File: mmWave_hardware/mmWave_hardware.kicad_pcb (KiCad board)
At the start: 2 copper layers, 1 part, among them U1 IWRL6432BDBAAMFR

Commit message: sch+pcb
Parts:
- added C1: 10p, Capacitor_SMD:C_0402_1005Metric_Pad0.74x0.62mm_HandSolder, B.Cu at (176.4, 112.5)
- added C10: 2u2, Capacitor_SMD:C_0603_1608Metric_Pad1.08x0.95mm_HandSolder, B.Cu at (181.3, 110.2)
- added C11: 10u, Capacitor_SMD:C_0603_1608Metric_Pad1.08x0.95mm_HandSolder, F.Cu at (177.8, 81.0)
- added C12: 2u2, Capacitor_SMD:C_0603_1608Metric_Pad1.08x0.95mm_HandSolder, F.Cu at (177.8, 83.5)
- added C13: 10u, Capacitor_SMD:C_0603_1608Metric_Pad1.08x0.95mm_HandSolder, B.Cu at (187.0, 118.3)
- added C14: 2u2, Capacitor_SMD:C_0603_1608Metric_Pad1.08x0.95mm_HandSolder, B.Cu at (187.0, 116.8)
- added C15: 47n, Capacitor_SMD:C_0402_1005Metric_Pad0.74x0.62mm_HandSolder, F.Cu at (179.8, 95.4)
- added C16: 1u, Capacitor_SMD:C_0603_1608Metric_Pad1.08x0.95mm_HandSolder, F.Cu at (182.1, 78.5)
- added C17: 1u, Capacitor_SMD:C_0603_1608Metric_Pad1.08x0.95mm_HandSolder, F.Cu at (182.1, 81.0)
- added C18: 10u, Capacitor_SMD:C_0603_1608Metric, F.Cu at (187.2, 106.4)
- added C19: 10u, Capacitor_SMD:C_0603_1608Metric, F.Cu at (193.6, 101.9)
- added C2: 10p, Capacitor_SMD:C_0402_1005Metric_Pad0.74x0.62mm_HandSolder, B.Cu at (176.5, 105.4)
- added C20: 10u, Capacitor_SMD:C_0603_1608Metric, F.Cu at (176.2, 91.0)
- added C21: 2u2, Capacitor_SMD:C_0603_1608Metric, F.Cu at (176.2, 93.5)
- added C3: 10u, Capacitor_SMD:C_0603_1608Metric_Pad1.08x0.95mm_HandSolder, B.Cu at (186.0, 112.2)
- added C4: 2u2, Capacitor_SMD:C_0603_1608Metric_Pad1.08x0.95mm_HandSolder, B.Cu at (186.0, 110.5)
- added C5: 10u, Capacitor_SMD:C_0603_1608Metric_Pad1.08x0.95mm_HandSolder, F.Cu at (178.9, 119.2)
- added C6: 2u2, Capacitor_SMD:C_0603_1608Metric_Pad1.08x0.95mm_HandSolder, F.Cu at (180.6, 119.2)
- added C7: 10u, Capacitor_SMD:C_0603_1608Metric_Pad1.08x0.95mm_HandSolder, F.Cu at (183.0, 119.1)
- added C8: 2u2, Capacitor_SMD:C_0603_1608Metric_Pad1.08x0.95mm_HandSolder, F.Cu at (184.8, 119.2)
- added C9: 10u, Capacitor_SMD:C_0603_1608Metric_Pad1.08x0.95mm_HandSolder, B.Cu at (183.0, 110.2)
- added J1: Conn_02x08_Top_Bottom, Connector_PinHeader_2.54mm:PinHeader_2x08_P2.54mm_Vertical, F.Cu at (209.4, 104.9)
- added R1: 10k, Resistor_SMD:R_0402_1005Metric, F.Cu at (172.7, 85.8)
- added R2: 100k, Resistor_SMD:R_0402_1005Metric, F.Cu at (172.7, 87.7)
- added R3: 100k, Resistor_SMD:R_0402_1005Metric, F.Cu at (172.7, 89.7)
- added R4: 10k, Resistor_SMD:R_0402_1005Metric, F.Cu at (172.7, 91.7)
- added R5: 10k, Resistor_SMD:R_0402_1005Metric, F.Cu at (172.7, 93.7)
- added R6: 10k, Resistor_SMD:R_0402_1005Metric, F.Cu at (172.7, 95.7)
- added TP1: TestPoint, TestPoint:TestPoint_Pad_D2.0mm, F.Cu at (161.6, 74.7)
- added TP2: TestPoint, TestPoint:TestPoint_Pad_D2.0mm, F.Cu at (161.6, 79.8)
- added TP3: TestPoint, TestPoint:TestPoint_Pad_D2.0mm, F.Cu at (161.6, 84.8)
- added TP4: TestPoint, TestPoint:TestPoint_Pad_D2.0mm, F.Cu at (161.6, 89.9)
- added TP5: TestPoint, TestPoint:TestPoint_Pad_D2.0mm, B.Cu at (189.5, 121.3)
- added U2: W25Q128JVS, Package_SO:SOIC-8_5.3x5.3mm_P1.27mm, F.Cu at (195.5, 108.1)
- added U3: AMS1117-3.3, Package_TO_SOT_SMD:SOT-223-3_TabPin2, F.Cu at (187.4, 101.1)
- added U4: TPS5430DDA, Package_SO:TI_SO-PowerPAD-8_ThermalVias, F.Cu at (147.1, 80.0)
- added Y1: 40.000, Crystal:Crystal_SMD_3225-4Pin_3.2x2.5mm_HandSoldering, B.Cu at (176.4, 109.0)
- moved U1 72.8 mm to (183.6, 113.5)
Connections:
- net Net-(U1-VSSA_PM) renamed GND
- U1 pad A10: unconnected-(U1-QSPI_CS-PadA10) -> /QSPI_CS
- U1 pad A11: unconnected-(U1-QSPI_CLK-PadA11) -> /QSPI_CLK
- U1 pad A3: unconnected-(U1-TX1-PadA3) -> TX1
- U1 pad A5: unconnected-(U1-TX2-PadA5) -> TX2
- U1 pad A7: unconnected-(U1-OSC_CLK_OUT-PadA7) -> Net-(U1-OSC_CLK_OUT)
- U1 pad B10: unconnected-(U1-QSPI[2]-PadB10) -> /QSPI_2
- U1 pad B11: unconnected-(U1-QSPI[0]-PadB11) -> /QSPI_0
- U1 pad B12: unconnected-(U1-SPIA_MOSI-PadB12) -> SPI0_MOSI
- U1 pad B8: unconnected-(U1-QSPI[1]-PadB8) -> /QSPI_2
- U1 pad B9: unconnected-(U1-QSPI[3]-PadB9) -> /QSPI_3
- U1 pad C11: unconnected-(U1-SPIA_MISO-PadC11) -> SPI0_MISO
- U1 pad C12: unconnected-(U1-TCK-PadC12) -> TCK
- U1 pad C6: unconnected-(U1-VIOIN_I8CLK-PadC6) -> 1v8
- U1 pad C8: unconnected-(U1-VIOIN_18-PadC8) -> 1v8
- U1 pad C9: unconnected-(U1-VDD-PadC9) -> 1v2
- U1 pad D10: unconnected-(U1-SPIA_CLK-PadD10) -> SPI0_CLK
- U1 pad D11: unconnected-(U1-SPIA_CS0_N-PadD11) -> SPI0_CS0_N
- U1 pad D3: unconnected-(U1-VOUT_14SYNTH-PadD3) -> Net-(U1-VOUT_14SYNTH)
- U1 pad E10: unconnected-(U1-RS232_TX-PadE10) -> RS232_TX
- U1 pad E11: unconnected-(U1-TDO-PadE11) -> TDO
- U1 pad E12: unconnected-(U1-TMS-PadE12) -> TMS
- U1 pad F1: unconnected-(U1-RX3-PadF1) -> RX3
- U1 pad F11: unconnected-(U1-RS232_RX-PadF11) -> RS232_RX
- U1 pad F3: unconnected-(U1-VDDA_18VCO-PadF3) -> 1v8
- U1 pad G11: unconnected-(U1-TDI-PadG11) -> TDI
- U1 pad G12: unconnected-(U1-VIOIN-PadG12) -> 3v3
- U1 pad G5: unconnected-(U1-VOUT_14APLL-PadG5) -> Net-(U1-VOUT_14APLL)
- U1 pad G7: unconnected-(U1-VDD-PadG7) -> 1v2
- U1 pad G8: unconnected-(U1-VDD-PadG8) -> 1v2
- U1 pad G9: unconnected-(U1-VDD-PadG9) -> 1v2
- U1 pad H1: unconnected-(U1-RX2-PadH1) -> RX2
- U1 pad H10: unconnected-(U1-GPIO_2-PadH10) -> GPIO_2
- U1 pad H11: unconnected-(U1-PMIC_CLKOUT-PadH11) -> Net-(U1-PMIC_CLKOUT)
- U1 pad H5: unconnected-(U1-VBGAP-PadH5) -> Net-(U1-VBGAP)
- U1 pad H8: unconnected-(U1-VDD-PadH8) -> 1v2
- U1 pad J10: unconnected-(U1-GPIO_5-PadJ10) -> GPIO_5
- U1 pad J11: unconnected-(U1-UARTA_RX-PadJ11) -> UART_RX
- U1 pad J5: unconnected-(U1-VIN_18PM-PadJ5) -> 1v8
- U1 pad K1: unconnected-(U1-RX1-PadK1) -> RX1
- U1 pad K11: unconnected-(U1-NERROR_OUT-PadK11) -> Net-(U1-NERROR_OUT)
- U1 pad K12: unconnected-(U1-VIOIN_18-PadK12) -> 1v8
- U1 pad K7: unconnected-(U1-VDD-PadK7) -> 1v2
- U1 pad L10: unconnected-(U1-NRESET-PadL10) -> NRST_MAIN
- U1 pad L11: unconnected-(U1-UARTA_RTS-PadL11) -> UART_RTS
- U1 pad L12: unconnected-(U1-UARTA_TX-PadL12) -> UART_TX
- U1 pad L3: unconnected-(U1-VDDA_10RF-PadL3) -> Net-(C5-Pad2)
- U1 pad L4: unconnected-(U1-VDDA_12RF-PadL4) -> Net-(C7-Pad1)
- U1 pad L5: unconnected-(U1-VDDA_18BB-PadL5) -> 1v8
- U1 pad L6: unconnected-(U1-GPADC2-PadL6) -> Net-(U1-GPADC2)
- U1 pad L8: unconnected-(U1-VIOIN_18-PadL8) -> 1v8
- U1 pad L9: unconnected-(U1-VNWA-PadL9) -> VDD_SRAM
- U1 pad M10: unconnected-(U1-HOST_CLK_REQ-PadM10) -> Net-(U1-HOST_CLK_REQ)
- U1 pad M11: unconnected-(U1-VIOIN-PadM11) -> 3v3
- U1 pad M3: unconnected-(U1-VDDA_10RF-PadM3) -> Net-(C5-Pad2)
- U1 pad M4: unconnected-(U1-VDDA_12RF-PadM4) -> Net-(C7-Pad1)
- U1 pad M5: unconnected-(U1-VDDA_18BB-PadM5) -> 1v8
- U1 pad M6: unconnected-(U1-GPADC1-PadM6) -> Net-(U1-GPADC1)
- U1 pad M7: unconnected-(U1-VDD_SRAM-PadM7) -> VDD_SRAM
- U1 pad M8: unconnected-(U1-VIOIN_18-PadM8) -> 1v8
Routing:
- net GND: track 13.0 -> 25.0 mm, vias 0 -> 9
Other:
- copper layers 2 -> 6

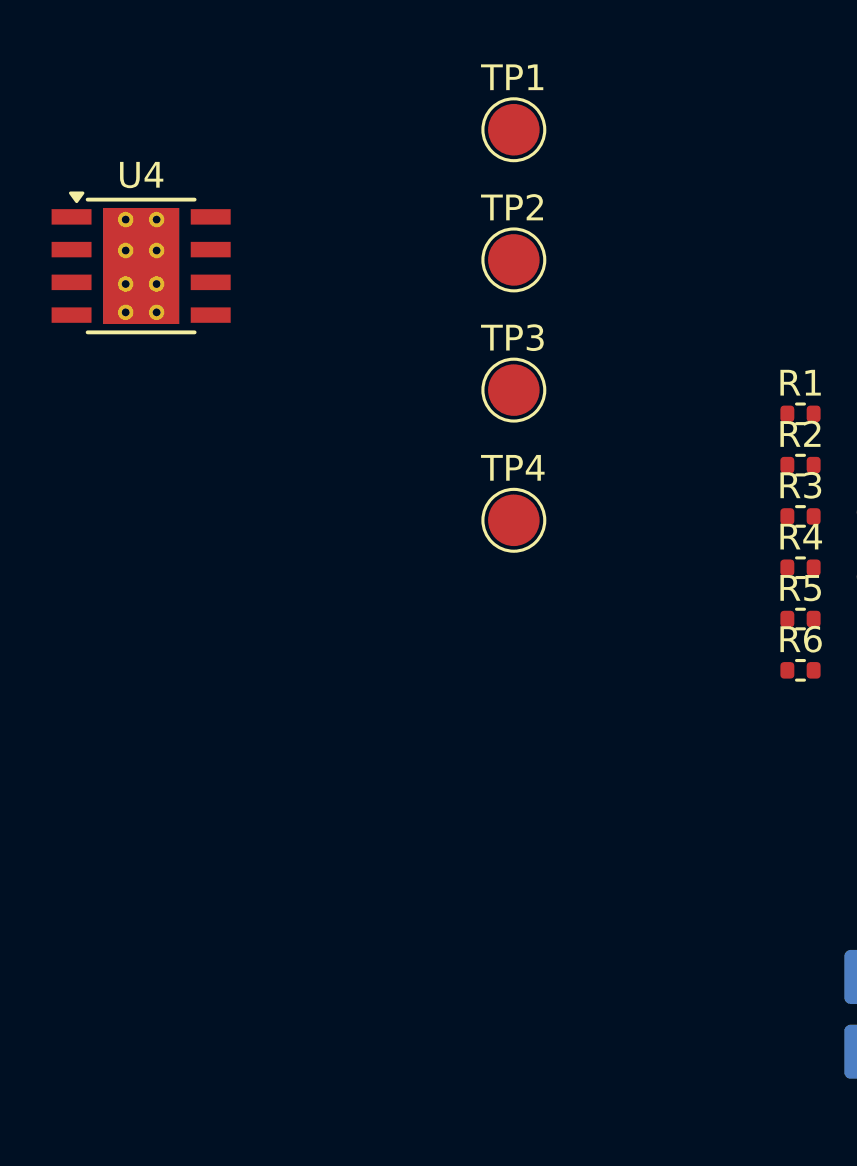
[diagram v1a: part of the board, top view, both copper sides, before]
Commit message: new buck conv
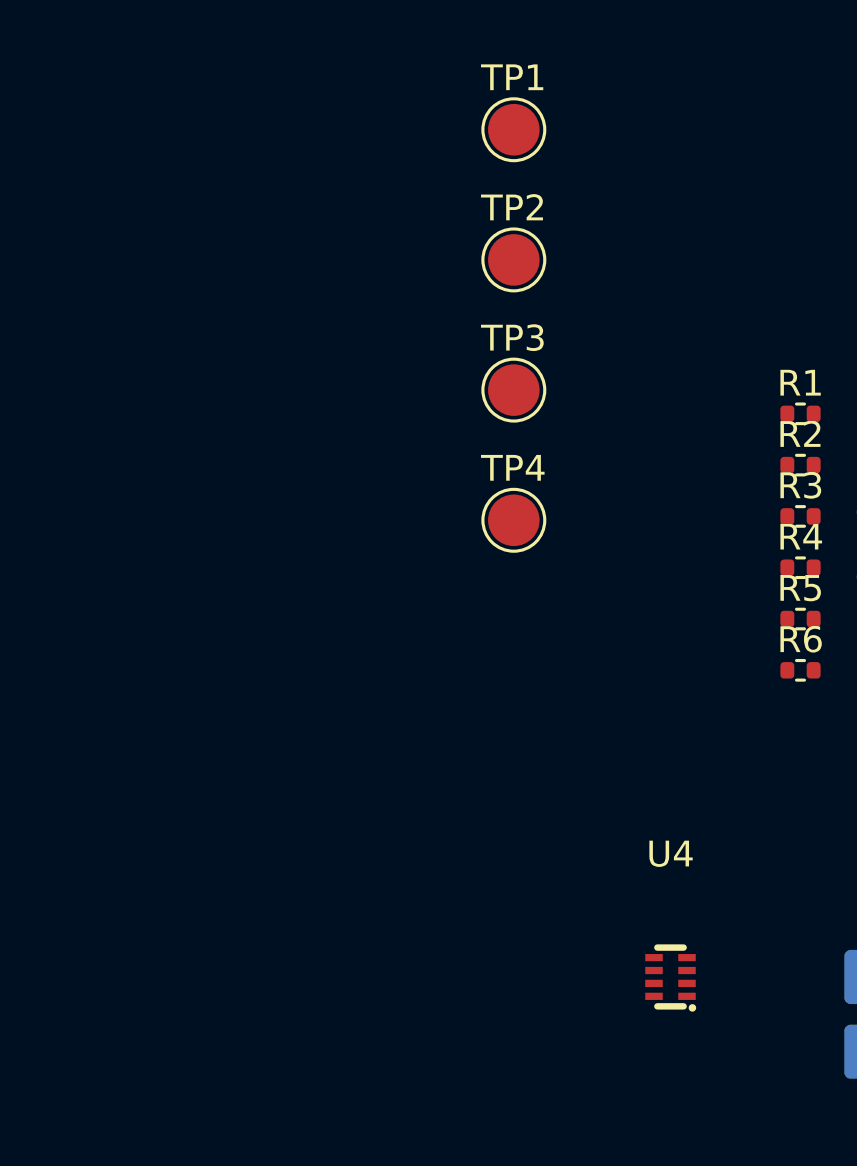
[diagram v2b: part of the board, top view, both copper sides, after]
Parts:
- C1, C2: value 10p -> 15p
- U4: value TPS5430DDA -> TPS628502QDRLRQ1; footprint Package_SO:TI_SO-PowerPAD-8_ThermalVias -> easyeda2kicad:SOT-583-8_L2.1-W1.2-P0.50-LS1.6-BR
- moved U4 34.4 mm to (167.7, 107.6)
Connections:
- U4 pad 1: unconnected-(U4-BOOT-Pad1) -> VIN
- U4 pad 2: unconnected-(U4-NC-Pad2) -> VIN
- U4 pad 5: VIN -> unconnected-(U4-FB-Pad5)
- U4 pad 6: GND -> unconnected-(U4-PG-Pad6)
- U4 pad 7: VIN -> unconnected-(U4-SW-Pad7)

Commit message: sch
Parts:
- C10, C13, C14, C3, C4, C9: moved to F.Cu
- C15: moved to B.Cu
- moved C15 20.3 mm to (183.8, 115.3), turned to 180 degrees
- moved C3 16.2 mm to (171.6, 119.5), turned to 180 degrees
- moved C4 16.2 mm to (171.6, 117.8), turned to 180 degrees
- moved C9 13.0 mm to (170.8, 114.7)
- moved C10 9.91 mm to (172.5, 114.7)
- moved C14 4.13 mm to (184.5, 120.1), turned to -90 degrees
- moved C8 2.06 mm to (182.9, 120.1)
- moved C13 2.06 mm to (186.2, 120.2), turned to -90 degrees
- moved C7 1.94 mm to (181.3, 120.1)
- moved C6 1.28 mm to (179.7, 120.1)
- moved C5 1.21 mm to (178.1, 120.1)
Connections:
- U1 pad B8: /QSPI_2 -> /QSPI_1
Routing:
- net GND: track 25.0 -> 12.6 mm, vias 9 -> 1
- net 1v8: track 0.00 -> 8.75 mm
- net Net-(C5-Pad2): track 0.00 -> 5.93 mm
- net Net-(C7-Pad1): track 0.00 -> 3.86 mm
- net 1v2: track 0.00 -> 1.50 mm

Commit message: sch+pcb
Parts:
- added C22: 10u, Capacitor_SMD:C_0603_1608Metric_Pad1.08x0.95mm_HandSolder, F.Cu at (196.7, 81.8)
- added C23: 10u, Capacitor_SMD:C_0603_1608Metric_Pad1.08x0.95mm_HandSolder, F.Cu at (196.7, 84.3)
- added C24: 10u, Capacitor_SMD:C_0603_1608Metric_Pad1.08x0.95mm_HandSolder, F.Cu at (196.7, 86.8)
- added C25: 10u, Capacitor_SMD:C_0603_1608Metric_Pad1.08x0.95mm_HandSolder, F.Cu at (196.7, 89.3)
- added R7: 100k, Resistor_SMD:R_0402_1005Metric, F.Cu at (200.3, 81.5)
- added R8: 18k, Resistor_SMD:R_0402_1005Metric, F.Cu at (200.3, 83.5)
- moved C15 1.14 mm to (183.2, 114.4)
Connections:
- U4 pad 3: unconnected-(U4-MODE/SYNC-Pad3) -> Net-(U4-MODE/SYNC)
- U4 pad 4: unconnected-(U4-COMP/FSET-Pad4) -> Net-(U4-COMP/FSET)
- U4 pad 5: unconnected-(U4-FB-Pad5) -> Net-(U4-FB)
- U4 pad 7: unconnected-(U4-SW-Pad7) -> Net-(U4-SW)
- U4 pad 8: unconnected-(U4-GND-Pad8) -> GND
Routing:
- net 1v8: track 8.75 -> 7.30 mm, vias 0 -> 1
- net UART_RTS: track 0.11 -> 0.79 mm, vias 0 -> 1
- net /QSPI_1: track 0.00 -> 0.68 mm, vias 0 -> 1
- net GND: track 12.6 -> 13.0 mm, vias 1 -> 2
- net Net-(U1-GPADC2): track 0.00 -> 0.07 mm, vias 0 -> 1
- net /QSPI_2: vias 0 -> 1

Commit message: sch+pcb
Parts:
- added L1: 470n, Inductor_SMD:L_0805_2012Metric_Pad1.05x1.20mm_HandSolder, F.Cu at (194.3, 114.0)
- added L2: 100n, Inductor_SMD:L_0805_2012Metric_Pad1.05x1.20mm_HandSolder, F.Cu at (194.3, 116.7)
- C1, C2: moved to F.Cu
- TP1, TP2, TP3, TP4, TP5: footprint TestPoint:TestPoint_Pad_D2.0mm -> TestPoint:TestPoint_Pad_D1.5mm
- moved J1 165.1 mm to (52.0, 55.3)
- moved C19 138.0 mm to (61.5, 61.8), turned to 0 degrees
- moved U3 130.4 mm to (61.5, 67.3), turned to 90 degrees
- moved C18 125.3 mm to (67.5, 69.7), turned to 90 degrees
- moved C13 123.7 mm to (73.2, 69.8), turned to 180 degrees
- moved C14 122.9 mm to (73.2, 68.1), turned to 180 degrees
- moved C8 122.1 mm to (73.2, 66.5), turned to 180 degrees
- moved C7 121.4 mm to (73.2, 64.9), turned to 180 degrees
- moved C6 120.7 mm to (73.2, 63.3), turned to 0 degrees
- moved C5 120.1 mm to (73.2, 61.7), turned to 0 degrees
- moved C15 114.6 mm to (78.9, 66.8), turned to 90 degrees
- moved U1 113.7 mm to (79.8, 67.2), turned to -90 degrees
- moved U2 111.8 mm to (90.1, 70.8)
- moved C1 107.8 mm to (81.8, 60.9), turned to -90 degrees
- moved Y1 104.4 mm to (83.2, 62.2), turned to 180 degrees
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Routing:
- net /QSPI_1: track 0.68 -> 0.05 mm, vias 1 -> 0
- net /CLKP: vias 0 -> 1
- net /CLKM: vias 0 -> 1
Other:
- board outline added: 50 x 1 mm

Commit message: layout
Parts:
- C16, C17, C20, C21, C22, C23, C24, C3, C4, L1, L2, R7, R8, TP1, TP2, TP3, TP4, U4: moved to B.Cu
- moved TP5 144.1 mm to (69.1, 58.7)
- moved L2 141.7 mm to (64.8, 59.4)
- moved R7 141.5 mm to (59.6, 67.5), turned to 90 degrees
- moved C24 139.6 mm to (60.2, 57.2)
- moved R8 139.5 mm to (62.1, 64.5), turned to 90 degrees
- moved L1 136.7 mm to (65.7, 67.8), turned to 90 degrees
- moved C23 134.9 mm to (64.7, 56.5)
- moved C22 129.5 mm to (68.0, 67.3), turned to -90 degrees
- moved R4 118.2 mm to (57.8, 64.2)
- moved C20 118.1 mm to (59.5, 73.0), turned to -90 degrees
- moved R5 117.8 mm to (57.9, 67.7)
- moved R6 116.9 mm to (57.9, 73.7)
- moved R3 116.2 mm to (57.9, 71.7), turned to 180 degrees
- moved R2 116.2 mm to (57.9, 70.3)
- moved C21 115.8 mm to (62.7, 70.1)
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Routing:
- net Net-(C7-Pad1): track 3.86 -> 7.74 mm
- net Net-(C5-Pad2): track 5.93 -> 2.11 mm
- net Net-(U1-VBGAP): track 0.00 -> 1.04 mm, vias 0 -> 1
- net 1v8: track 7.30 -> 8.20 mm
- net UART_RTS: track 0.79 -> 0.11 mm
- net Net-(U1-GPADC1): track 0.00 -> 0.49 mm, vias 0 -> 1
- net Net-(U1-VOUT_14SYNTH): track 0.00 -> 0.22 mm, vias 0 -> 1
- net Net-(U1-NERROR_OUT): track 0.00 -> 0.19 mm, vias 0 -> 1
- net Net-(U1-HOST_CLK_REQ): track 0.00 -> 0.10 mm, vias 0 -> 1
- net NRST_MAIN: vias 0 -> 1

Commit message: antennaaaaaaaaaaaaaaaaaaaaa
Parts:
- added C18: 10u, Capacitor_SMD:C_0603_1608Metric, F.Cu at (1.50, 0.76)
- added C19: 10u, Capacitor_SMD:C_0603_1608Metric, F.Cu at (1.50, 3.27)
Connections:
- C3 pad 2: Net-(C3-Pad2) -> GND
- C4 pad 2: Net-(C3-Pad2) -> GND

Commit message: antennaaaaaaaaaaaaaaaaaaaaa
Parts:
- added AE1: Antenna, antennas:60GHz_microstrip_inset_patch, F.Cu at (88.4, 60.2)
- added AE2: Antenna, antennas:60GHz_microstrip_inset_patch, F.Cu at (78.2, 57.3)
- added AE3: Antenna, antennas:60GHz_microstrip_inset_patch, F.Cu at (81.0, 57.3)
- added AE4: Antenna, antennas:60GHz_microstrip_inset_patch, F.Cu at (83.7, 57.3)
- added AE5: Antenna, antennas:60GHz_microstrip_inset_patch, F.Cu at (86.5, 57.3)
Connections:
- U1 pad A3: TX1 -> Net-(AE2-A)
- U1 pad A5: TX2 -> Net-(AE1-A)
- U1 pad F1: RX3 -> Net-(AE3-A)
- U1 pad H1: RX2 -> Net-(AE4-A)
- U1 pad K1: RX1 -> Net-(AE5-A)
